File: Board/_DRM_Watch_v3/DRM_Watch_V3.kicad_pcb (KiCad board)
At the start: 2 copper layers, 62.7 x 44.4 mm, 116 parts, among them J1 TYPE-C-31-M-12, J2 FPC 10pin 0.5mm pitch, M1 M1.2 screw mount get from DJI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, M2 M1.2 screw mount get from DJI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, M3 M1.2 screw mount get from DJI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, Q1 2N7002LT1G (SOT-23-3), Q2 2N7002LT1G (SOT-23-3), U1 ESP32-S2, U2 ME6211 SOT23-5 3.3V, U3 TP4056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

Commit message: 2024-06-22 v2.32  Збільшено кількість точок що додаються на один кадр 2024-06-22 v2.32  Реалізовано: Перед вимкненням по таймеру щоб ліхтар мигав щосекунди 2024-06-22 v2.32  Реалізовано: якщо годинник в глибокому розряді - не стартувати а відправлятись одразу в сон 2024-06-22 v2.32  Додана мелодія: Angry birds 2024-06-22 v2.32  Доповнено документацію
2024-06-22 v2.32  Збільшено кількість точок що додаються на один кадр
2024-06-22 v2.32  Реалізовано: Перед вимкненням по таймеру щоб ліхтар мигав щосекунди
2024-06-22 v2.32  Реалізовано: якщо годинник в глибокому розряді - не стартувати а відправлятись одразу в сон
2024-06-22 v2.32  Додана мелодія: Angry birds
2024-06-22 v2.32  Доповнено документацію
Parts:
- R9: value 10K -> 2K
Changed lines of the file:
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@@
         (effects (font (size 0.1 0.1) (thickness 0.025)))
     )
-    (fp_text value "10K" (at 1.143 0.508 -90 unlocked) (layer "F.Fab")
+    (fp_text value "2K" (at 1.143 0.508 -90 unlocked) (layer "F.Fab")
         (effects (font (size 0.2 0.2) (thickness 0.025)) (justify right bottom))
     )

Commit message: 2024-06-29 v2.33  Виправлено помилку - тип мікросхеми в схемі і на платі 2024-06-29 v2.33  Дописано флешер для Windows 2024-06-29 v2.33  Доповнено документацію
2024-06-29 v2.33  Виправлено помилку - тип мікросхеми в схемі і на платі
2024-06-29 v2.33  Дописано флешер для Windows
2024-06-29 v2.33  Доповнено документацію
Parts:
- U1: value ESP32-S2 -> ESP32-S2FN4R2
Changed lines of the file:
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@@
     (descr "QFN, 56 Pin (https://www.espressif.com/sites/default/files/documentation/esp32-s2_datasheet_en.pdf#page=41), generated with kicad-footprint-generator ipc_noLead_generator.py")
     (tags "QFN NoLead")
-    (property "Description" "ESP32-S2 Programmable Microcontroller Chip")
+    (property "Description" "ESP32-S2FN4R2 Programmable Microcontroller Chip")
     (property "Link" "https://www.tme.eu/en/details/esp32s2/iot-wifi-bluetooth-modules/espressif/esp32-s2/")
     (property "Manufacturer" "Espressif")
@@
         (effects (font (size 0.2 0.2) (thickness 0.0375)))
     )
-    (fp_text value "ESP32-S2" (at -0.0254 2.5146) (layer "F.Fab")
+    (fp_text value "ESP32-S2FN4R2" (at -0.0254 2.5146) (layer "F.Fab")
         (effects (font (size 0.1 0.1) (thickness 0.025)))
     )
-    (fp_text user "ESP32-S2" (at 0 0 unlocked) (layer "F.Fab")
-        (effects (font (size 0.6 0.6) (thickness 0.15)))
+    (fp_text user "ESP32-S2FN4R2" (at 0 0 unlocked) (layer "F.Fab")
+        (effects (font (size 0.5 0.5) (thickness 0.125)))
     )
     (fp_text user "${REFERENCE}" (at 0 -2.2098) (layer "F.Fab") hide
@@
     (fp_circle (center -3.429 -3.429) (end -3.302 -3.429)
       (stroke (width 0.1) (type solid)) (fill solid) (layer "F.Fab"))
-    (pad "" smd roundrect (at -0.875 -0.875) (size 1.549193 1.549193) (layers "F.Paste") (roundrect_rratio 0.1613736959))
-    (pad "" smd roundrect (at -0.875 0.875) (size 1.549193 1.549193) (layers "F.Paste") (roundrect_rratio 0.1613736959))
-    (pad "" smd roundrect (at 0.875 -0.875) (size 1.549193 1.549193) (layers "F.Paste") (roundrect_rratio 0.1613736959))
-    (pad "" smd roundrect (at 0.875 0.875) (size 1.549193 1.549193) (layers "F.Paste") (roundrect_rratio 0.1613736959))
+    (pad "" smd roundrect (at -0.875 -0.875) (size 1.549193 1.549193) (layers "F.Paste") (roundrect_rratio 0.161374))
+    (pad "" smd roundrect (at -0.875 0.875) (size 1.549193 1.549193) (layers "F.Paste") (roundrect_rratio 0.161374))
+    (pad "" smd roundrect (at 0.875 -0.875) (size 1.549193 1.549193) (layers "F.Paste") (roundrect_rratio 0.161374))
+    (pad "" smd roundrect (at 0.875 0.875) (size 1.549193 1.549193) (layers "F.Paste") (roundrect_rratio 0.161374))
     (pad "1" smd roundrect (at -3.45 -2.6) (size 0.8 0.2) (layers "F.Cu" "F.Paste" "F.Mask") (roundrect_rratio 0.25)
       (net 3 "+3V3") (pinfunction "VDDA") (pintype "power_in"))

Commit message: 2024-06-29 v2.33  В схемі виправлено хибне посилання на невірний кварц
2024-06-29 v2.33  В схемі виправлено хибне посилання на невірний кварц
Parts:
- Y1: footprint Project-Lib:OSC_XRCGB48M000F0Z00R0 -> Project-Lib:Oscilator
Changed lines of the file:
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@@
     )
   )
-  (footprint "Project-Lib:OSC_XRCGB48M000F0Z00R0" (layer "F.Cu")
+  (footprint "Project-Lib:Oscilator" (layer "F.Cu")
     (at 116.020503 46.426716 90)
     (property "Description" "SMD 3225 4PIN 40Mhz 3.2*2.5mm Passive SMD Quartz Resonator 40.000Mhz")
     (property "Link" "https://www.aliexpress.us/item/1005004689346275.html")
-    (property "Manufacturer" "Murata Electronics")
     (property "Role" "Frequency Oscilator")
     (property "Sheetfile" "DRM_Watch_V3.kicad_sch")
     (property "Sheetname" "")
+    (property "ki_description" "SMD 3225 4PIN 40Mhz 3.2*2.5mm Passive SMD Quartz Resonator 40.000Mhz")
     (attr smd)
     (fp_text reference "Y1" (at 0 0 90) (layer "F.Fab")

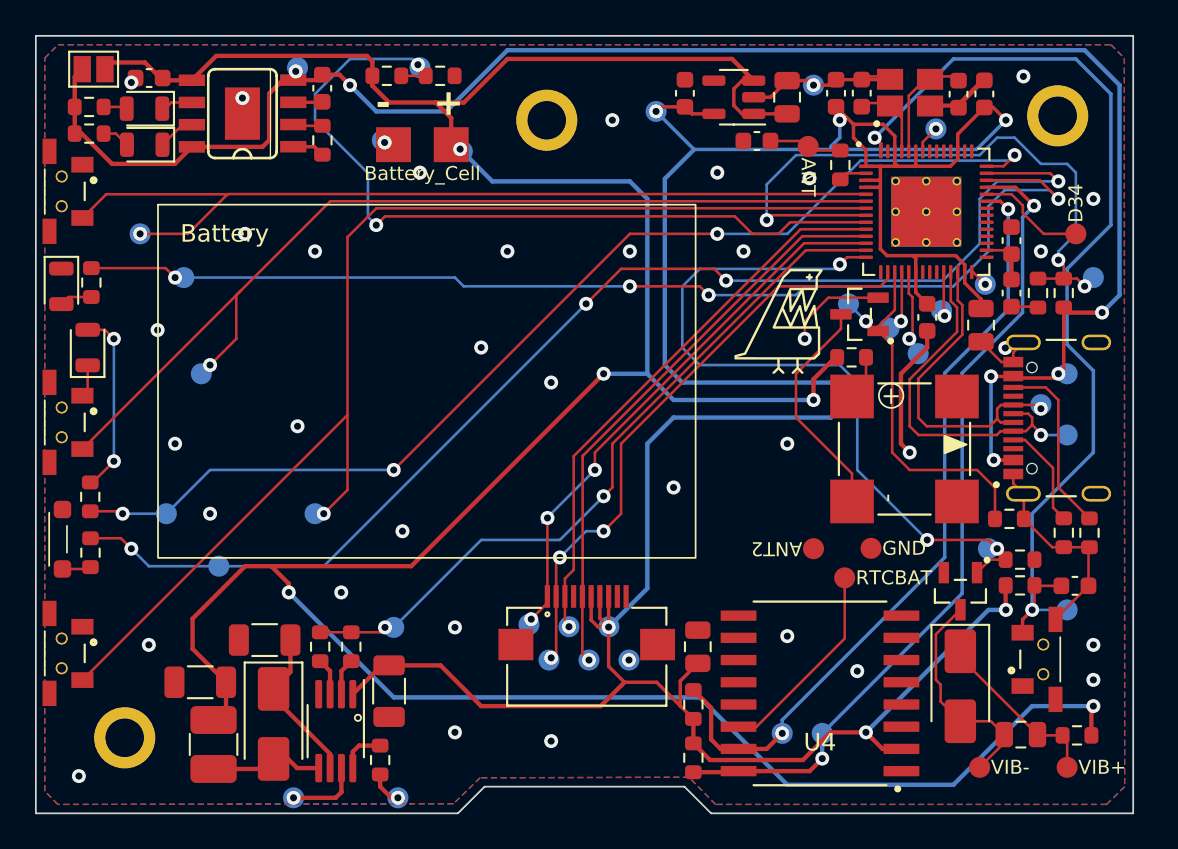
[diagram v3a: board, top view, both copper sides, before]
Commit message: 2024-06-30 v2.33  Виправлена інформація про гайки на платі:  Brass SMTSO-M1.4X3X1.5-2X0.8
2024-06-30 v2.33  Виправлена інформація про гайки на платі:  Brass SMTSO-M1.4X3X1.5-2X0.8
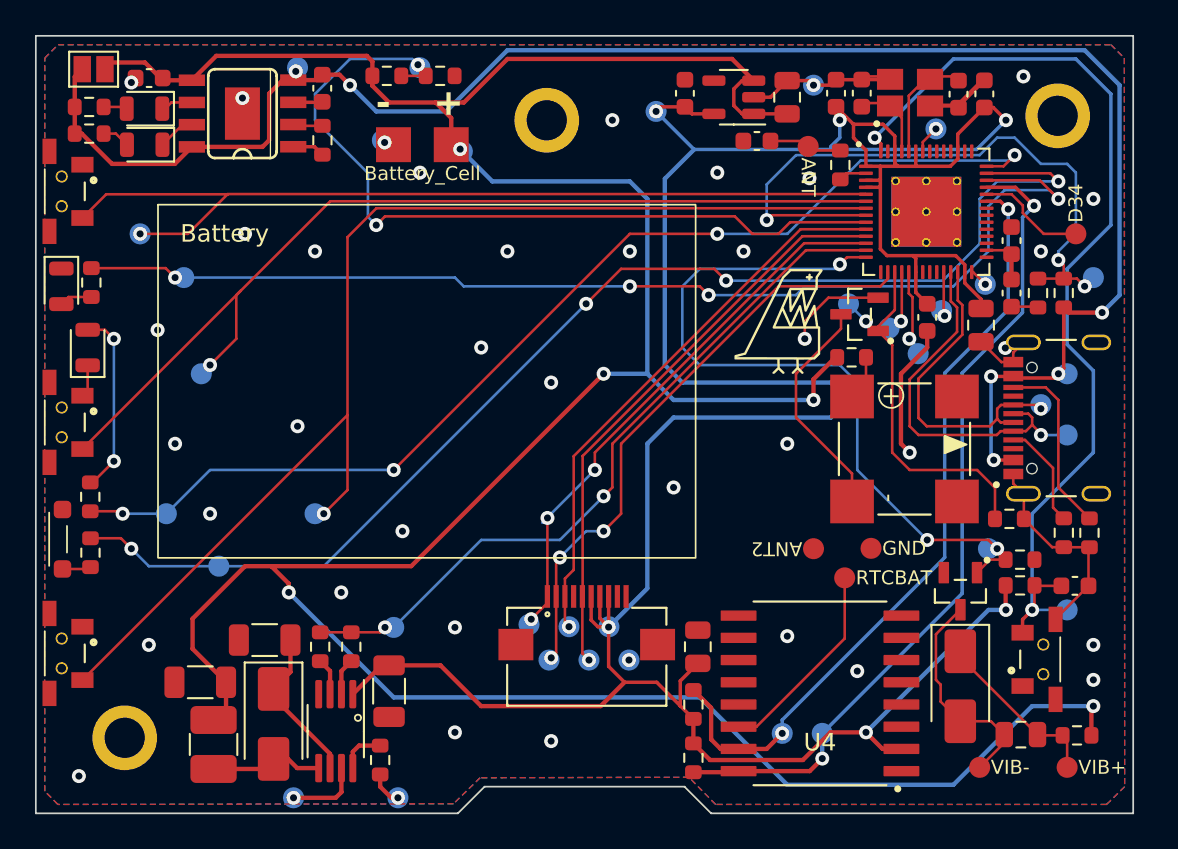
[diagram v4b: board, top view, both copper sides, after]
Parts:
- M1, M2, M3: value M1.2 screw mount get from DJI Mavic 3 CORE board -> Brass SMTSO-M1.4X3X1.5-2X0.8; footprint Project-Lib:m1.2-screw-mount -> Project-Lib:m1.4-screw-mount
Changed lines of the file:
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@@
       (net 55 "unconnected-(TP28-Pad1)") (pinfunction "1") (pintype "passive"))
   )
-  (footprint "Project-Lib:m1.2-screw-mount" (layer "F.Cu")
+  (footprint "Project-Lib:m1.4-screw-mount" (layer "F.Cu")
     (at 124.46 47.752)
-    (property "Description" "Surface mount spacers with thread")
-    (property "Link" "https://www.aliexpress.com/i/1005005125674149.html   (SMTSO-M1.2-2)")
+    (property "Description" "M1.4 screw mount get from DJI Mavic 3 CORE board")
+    (property "Link" "https://www.aliexpress.com/item/1005005579653583.html")
     (property "Role" "Screw mount for back case")
     (property "Sheetfile" "DRM_Watch_V3.kicad_sch")
     (property "Sheetname" "")
+    (property "ki_description" "M1.4 screw mount get from DJI Mavic 3 CORE board")
     (attr smd)
     (fp_text reference "M2" (at 0.254 -8.358 unlocked) (layer "F.SilkS") hide
         (effects (font (size 1 1) (thickness 0.1)))
     )
-    (fp_text value "M1.2 screw mount get from DJI Mavic 3 CORE board" (at 0.254 -6.858 unlocked) (layer "F.Fab") hide
+    (fp_text value "Brass SMTSO-M1.4X3X1.5-2X0.8" (at 0.254 -6.858 unlocked) (layer "F.Fab") hide
         (effects (font (size 1 1) (thickness 0.15)))
     )
@@
     (fp_circle (center 0 0) (end 2 0)
       (stroke (width 0.05) (type default)) (fill none) (layer "F.CrtYd"))
-    (pad "1" thru_hole circle (at 0 0) (size 3.5 3.5) (drill 2.2) (layers "*.Cu" "*.Mask" "Eco2.User")
+    (pad "1" thru_hole circle (at 0 0) (size 3.7 3.7) (drill 2.3) (layers "*.Cu" "*.Mask" "Eco2.User")
       (net 24 "GND") (pintype "passive") (solder_mask_margin 0.3))
     (model "../ScrewMount/M1.2 Screw Mount v9.step"
@@
       (net 50 "Net-(C13-Pad2)") (pinfunction "1") (pintype "passive"))
   )
-  (footprint "Project-Lib:m1.2-screw-mount" (layer "F.Cu")
+  (footprint "Project-Lib:m1.4-screw-mount" (layer "F.Cu")
     (at 95.25 48.006)
-    (property "Description" "Surface mount spacers with thread")
-    (property "Link" "https://www.aliexpress.com/i/1005005125674149.html   (SMTSO-M1.2-2)")
+    (property "Description" "M1.4 screw mount get from DJI Mavic 3 CORE board")
+    (property "Link" "https://www.aliexpress.com/item/1005005579653583.html")
     (property "Role" "Screw mount for back case")
     (property "Sheetfile" "DRM_Watch_V3.kicad_sch")
     (property "Sheetname" "")
+    (property "ki_description" "M1.4 screw mount get from DJI Mavic 3 CORE board")
     (attr smd)
     (fp_text reference "M3" (at 0.254 -8.358 unlocked) (layer "F.SilkS") hide
         (effects (font (size 1 1) (thickness 0.1)))
     )
-    (fp_text value "M1.2 screw mount get from DJI Mavic 3 CORE board" (at 0.254 -6.858 unlocked) (layer "F.Fab") hide
+    (fp_text value "Brass SMTSO-M1.4X3X1.5-2X0.8" (at 0.254 -6.858 unlocked) (layer "F.Fab") hide
         (effects (font (size 1 1) (thickness 0.15)))
     )
@@
     (fp_circle (center 0 0) (end 2 0)
       (stroke (width 0.05) (type default)) (fill none) (layer "F.CrtYd"))
-    (pad "1" thru_hole circle (at 0 0) (size 3.5 3.5) (drill 2.2) (layers "*.Cu" "*.Mask" "Eco2.User")
+    (pad "1" thru_hole circle (at 0 0) (size 3.7 3.7) (drill 2.3) (layers "*.Cu" "*.Mask" "Eco2.User")
       (net 24 "GND") (pintype "passive") (solder_mask_margin 0.3))
     (model "../ScrewMount/M1.2 Screw Mount v9.step"
@@
       (net 24 "GND") (pinfunction "1") (pintype "passive"))
   )
-  (footprint "Project-Lib:m1.2-screw-mount" (layer "F.Cu")
+  (footprint "Project-Lib:m1.4-screw-mount" (layer "F.Cu")
     (at 71.12 83.312)
-    (property "Description" "Surface mount spacers with thread")
-    (property "Link" "https://www.aliexpress.com/i/1005005125674149.html   (SMTSO-M1.2-2)")
+    (property "Description" "M1.4 screw mount get from DJI Mavic 3 CORE board")
+    (property "Link" "https://www.aliexpress.com/item/1005005579653583.html")
     (property "Role" "Screw mount for back case")
     (property "Sheetfile" "DRM_Watch_V3.kicad_sch")
     (property "Sheetname" "")
+    (property "ki_description" "M1.4 screw mount get from DJI Mavic 3 CORE board")
     (attr smd)
     (fp_text reference "M1" (at 0.254 -8.358 unlocked) (layer "F.SilkS") hide
         (effects (font (size 1 1) (thickness 0.1)))
     )
-    (fp_text value "M1.2 screw mount get from DJI Mavic 3 CORE board" (at 0.254 -6.858 unlocked) (layer "F.Fab") hide
+    (fp_text value "Brass SMTSO-M1.4X3X1.5-2X0.8" (at 0.254 -6.858 unlocked) (layer "F.Fab") hide
         (effects (font (size 1 1) (thickness 0.15)))
     )
@@
     (fp_circle (center 0 0) (end 2 0)
       (stroke (width 0.05) (type default)) (fill none) (layer "F.CrtYd"))
-    (pad "1" thru_hole circle (at 0 0) (size 3.5 3.5) (drill 2.2) (layers "*.Cu" "*.Mask" "Eco2.User")
+    (pad "1" thru_hole circle (at 0 0) (size 3.7 3.7) (drill 2.3) (layers "*.Cu" "*.Mask" "Eco2.User")
       (net 24 "GND") (pintype "passive") (solder_mask_margin 0.3))
     (model "../ScrewMount/M1.2 Screw Mount v9.step"
